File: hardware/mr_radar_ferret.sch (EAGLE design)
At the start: 66 parts, among them U1 GALI-55+, U10 MAX2750, U11 GALI-55+, U12 AD5621, U13 REF2930, U3 GALI-55+, U4 GALI-55+, U7 DC25-73, U8 HMC213

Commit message: mr_radar_ferret r0, sent for manufacturing
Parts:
- R22: value 110 -> JMP
- R23: value 110 -> DNP
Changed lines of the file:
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@@
 <part name="SUPPLY6" library="supply2" deviceset="+10V" device=""/>
 <part name="GND65" library="supply1" deviceset="GND" device=""/>
-<part name="R22" library="pel_dipol_comp" deviceset="RESISTOR" device="-0603" value="110"/>
+<part name="R22" library="pel_dipol_comp" deviceset="RESISTOR" device="-0603" value="JMP"/>
 <part name="P+18" library="supply1" deviceset="+5V" device=""/>
-<part name="R23" library="pel_dipol_comp" deviceset="RESISTOR" device="-0603" value="110"/>
+<part name="R23" library="pel_dipol_comp" deviceset="RESISTOR" device="-0603" value="DNP"/>
 <part name="GND70" library="supply1" deviceset="GND" device=""/>
 </parts>
@@
 <instance part="GND39" gate="1" x="-170.18" y="-71.12" rot="R90"/>
 <instance part="JP1" gate="G$1" x="-193.04" y="-73.66"/>
-<instance part="P+13" gate="1" x="81.28" y="109.22"/>
+<instance part="P+13" gate="1" x="78.74" y="101.6"/>
 <instance part="C30" gate="G$1" x="78.74" y="88.9"/>
 <instance part="GND47" gate="1" x="78.74" y="78.74"/>
@@
 <instance part="GND61" gate="1" x="53.34" y="78.74"/>
 <instance part="C20" gate="G$1" x="-20.32" y="-76.2"/>
-<instance part="P+14" gate="1" x="-20.32" y="-71.12"/>
-<instance part="GND62" gate="1" x="-20.32" y="-83.82"/>
+<instance part="P+14" gate="1" x="-20.32" y="-68.58"/>
+<instance part="GND62" gate="1" x="-20.32" y="-86.36"/>
 <instance part="J$5" gate="1" x="175.26" y="119.38" rot="MR0"/>
 <instance part="GND63" gate="1" x="180.34" y="99.06"/>
@@
 <pinref part="C20" gate="G$1" pin="2"/>
 <pinref part="GND62" gate="1" pin="GND"/>
+<wire x1="-20.32" y1="-83.82" x2="-20.32" y2="-81.28" width="0.1524" layer="91"/>
 </segment>
 <segment>
@@
 <segment>
 <pinref part="P+13" gate="1" pin="+5V"/>
-<wire x1="81.28" y1="106.68" x2="81.28" y2="99.06" width="0.1524" layer="91"/>
-<wire x1="81.28" y1="99.06" x2="78.74" y2="96.52" width="0.1524" layer="91"/>
 <pinref part="C30" gate="G$1" pin="+"/>
-<wire x1="78.74" y1="96.52" x2="78.74" y2="91.44" width="0.1524" layer="91"/>
+<wire x1="78.74" y1="99.06" x2="78.74" y2="91.44" width="0.1524" layer="91"/>
 </segment>
 <segment>
 <pinref part="C20" gate="G$1" pin="1"/>
 <pinref part="P+14" gate="1" pin="+5V"/>
-</segment>
-<segment>
+<wire x1="-20.32" y1="-71.12" x2="-20.32" y2="-73.66" width="0.1524" layer="91"/>
+</segment>
+<segment>

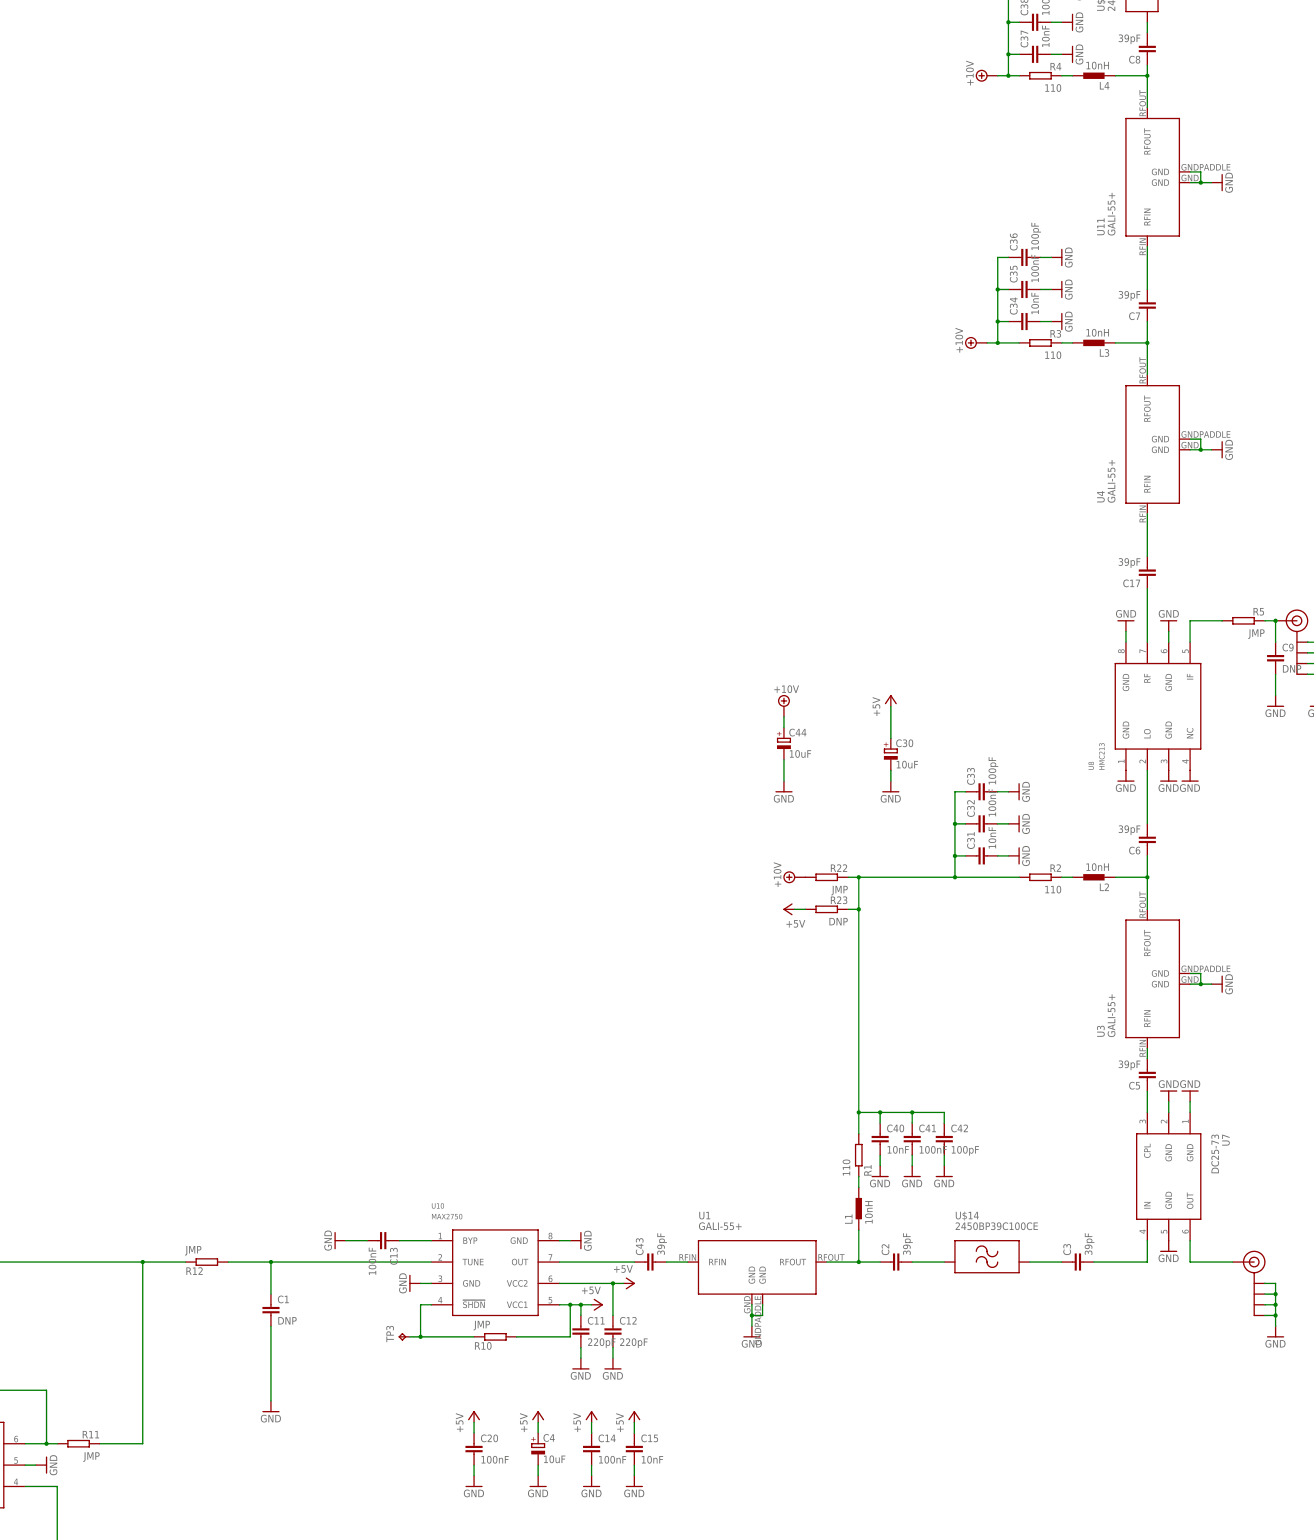
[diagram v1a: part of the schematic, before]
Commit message: currently tested ferret r0, fixing a few bugs for the next revision, board layout of ferret now incomplete. isolation is much better than in platypus, but it is still a problem
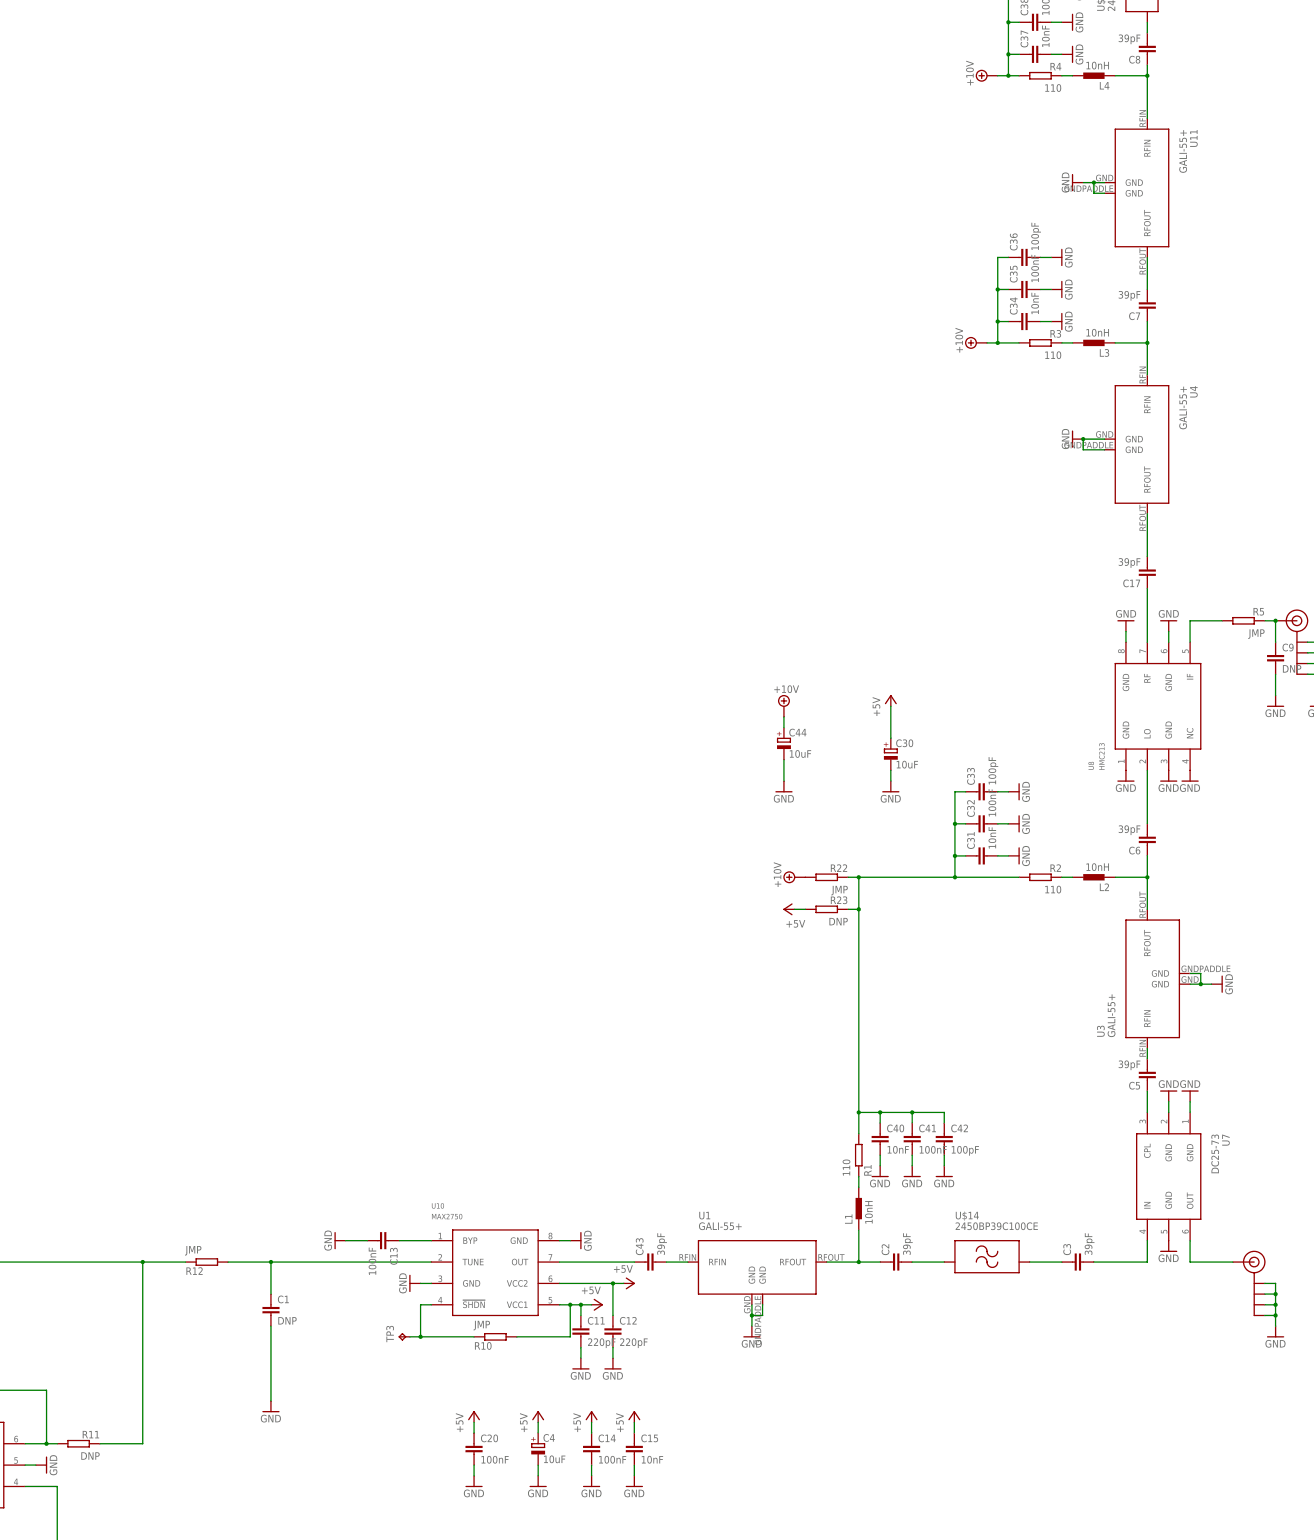
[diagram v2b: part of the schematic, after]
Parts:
- R11: value JMP -> DNP
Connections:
- removed net N$19: C7.2, U11.RFIN
- removed net N$29: C17.2, U4.RFIN
- new net N$23: C7.2, U11.RFOUT
- new net N$9: C17.2, U4.RFOUT
- net N$18: now also U4.RFIN; no longer U4.RFOUT
- net N$20: now also U11.RFIN; no longer U11.RFOUT
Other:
- moved on the sheet: U11, U4
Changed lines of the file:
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@@
 <part name="GND37" library="supply1" deviceset="GND" device=""/>
 <part name="GND38" library="supply1" deviceset="GND" device=""/>
-<part name="R11" library="pel_dipol_comp" deviceset="RESISTOR" device="-0603" value="JMP"/>
+<part name="R11" library="pel_dipol_comp" deviceset="RESISTOR" device="-0603" value="DNP"/>
 <part name="GND39" library="supply1" deviceset="GND" device=""/>
 <part name="JP1" library="SparkFun-Connectors" deviceset="M05" device="PTH"/>
@@
 <instance part="GND9" gate="1" x="134.62" y="119.38" rot="R180"/>
 <instance part="GND10" gate="1" x="144.78" y="119.38" rot="R180"/>
-<instance part="U4" gate="G$1" x="142.24" y="160.02" rot="R90"/>
+<instance part="U4" gate="G$1" x="137.16" y="162.56" rot="R270"/>
 <instance part="R3" gate="G$1" x="114.3" y="185.42" rot="R180"/>
 <instance part="L3" gate="G$1" x="127" y="185.42" rot="R90"/>
-<instance part="GND11" gate="1" x="157.48" y="160.02" rot="R90"/>
+<instance part="GND11" gate="1" x="121.92" y="162.56" rot="R270"/>
 <instance part="C7" gate="G$1" x="139.7" y="193.04" rot="R180"/>
 <instance part="SUPPLY3" gate="G$1" x="99.06" y="185.42" rot="R90"/>
-<instance part="U11" gate="G$1" x="142.24" y="223.52" rot="R90"/>
+<instance part="U11" gate="G$1" x="137.16" y="223.52" rot="R270"/>
 <instance part="R4" gate="G$1" x="114.3" y="248.92" rot="R180"/>
 <instance part="L4" gate="G$1" x="127" y="248.92" rot="R90"/>
-<instance part="GND12" gate="1" x="157.48" y="223.52" rot="R90"/>
+<instance part="GND12" gate="1" x="121.92" y="223.52" rot="R270"/>
 <instance part="C8" gate="G$1" x="139.7" y="254" rot="R180"/>
 <instance part="SUPPLY4" gate="G$1" x="101.6" y="248.92" rot="R90"/>
@@
 </segment>
 <segment>
-<pinref part="GND11" gate="1" pin="GND"/>
-<pinref part="U4" gate="G$1" pin="GND@0"/>
-<wire x1="154.94" y1="160.02" x2="152.4" y2="160.02" width="0.1524" layer="91"/>
-<pinref part="U4" gate="G$1" pin="GND@1"/>
-<wire x1="152.4" y1="160.02" x2="149.86" y2="160.02" width="0.1524" layer="91"/>
-<wire x1="149.86" y1="162.56" x2="152.4" y2="162.56" width="0.1524" layer="91"/>
-<wire x1="152.4" y1="162.56" x2="152.4" y2="160.02" width="0.1524" layer="91"/>
-<junction x="152.4" y="160.02"/>
-</segment>
-<segment>
 <pinref part="GND12" gate="1" pin="GND"/>
 <pinref part="U11" gate="G$1" pin="GND@0"/>
-<wire x1="154.94" y1="223.52" x2="152.4" y2="223.52" width="0.1524" layer="91"/>
+<wire x1="124.46" y1="223.52" x2="127" y2="223.52" width="0.1524" layer="91"/>
 <pinref part="U11" gate="G$1" pin="GND@1"/>
-<wire x1="152.4" y1="223.52" x2="149.86" y2="223.52" width="0.1524" layer="91"/>
-<wire x1="149.86" y1="226.06" x2="152.4" y2="226.06" width="0.1524" layer="91"/>
-<wire x1="152.4" y1="226.06" x2="152.4" y2="223.52" width="0.1524" layer="91"/>
-<junction x="152.4" y="223.52"/>
+<wire x1="127" y1="223.52" x2="129.54" y2="223.52" width="0.1524" layer="91"/>
+<wire x1="129.54" y1="220.98" x2="127" y2="220.98" width="0.1524" layer="91"/>
+<wire x1="127" y1="220.98" x2="127" y2="223.52" width="0.1524" layer="91"/>
+<junction x="127" y="223.52"/>
 </segment>
 <segment>
@@
 <pinref part="GND70" gate="1" pin="GND"/>
 </segment>
+<segment>
+<pinref part="GND11" gate="1" pin="GND"/>
+<pinref part="U4" gate="G$1" pin="GND@0"/>
+<wire x1="124.46" y1="162.56" x2="129.54" y2="162.56" width="0.1524" layer="91"/>
+<pinref part="U4" gate="G$1" pin="GND@1"/>
+<wire x1="129.54" y1="160.02" x2="124.46" y2="160.02" width="0.1524" layer="91"/>
+<wire x1="124.46" y1="160.02" x2="124.46" y2="162.56" width="0.1524" layer="91"/>
+<junction x="124.46" y="162.56"/>
+</segment>
 </net>
 <net name="N$2" class="0">
@@
 <net name="N$18" class="0">
 <segment>
-<pinref part="U4" gate="G$1" pin="RFOUT"/>
 <pinref part="C7" gate="G$1" pin="1"/>
-<wire x1="139.7" y1="177.8" x2="139.7" y2="185.42" width="0.1524" layer="91"/>
 <pinref part="L3" gate="G$1" pin="2"/>
 <wire x1="139.7" y1="185.42" x2="139.7" y2="190.5" width="0.1524" layer="91"/>
 <wire x1="132.08" y1="185.42" x2="139.7" y2="185.42" width="0.1524" layer="91"/>
+<pinref part="U4" gate="G$1" pin="RFIN"/>
+<wire x1="139.7" y1="177.8" x2="139.7" y2="185.42" width="0.1524" layer="91"/>
 <junction x="139.7" y="185.42"/>
 </segment>
@@
 <net name="N$20" class="0">
 <segment>
-<pinref part="U11" gate="G$1" pin="RFOUT"/>
 <pinref part="C8" gate="G$1" pin="1"/>
-<wire x1="139.7" y1="241.3" x2="139.7" y2="248.92" width="0.1524" layer="91"/>
 <pinref part="L4" gate="G$1" pin="2"/>
 <wire x1="139.7" y1="248.92" x2="139.7" y2="251.46" width="0.1524" layer="91"/>
 <wire x1="132.08" y1="248.92" x2="139.7" y2="248.92" width="0.1524" layer="91"/>
+<wire x1="139.7" y1="238.76" x2="139.7" y2="248.92" width="0.1524" layer="91"/>
 <junction x="139.7" y="248.92"/>
-</segment>
-</net>
-<net name="N$19" class="0">
-<segment>
 <pinref part="U11" gate="G$1" pin="RFIN"/>
-<wire x1="139.7" y1="208.28" x2="139.7" y2="198.12" width="0.1524" layer="91"/>
-<pinref part="C7" gate="G$1" pin="2"/>
 </segment>
 </net>
@@
 <pinref part="U8" gate="G$1" pin="RF@7"/>
 <wire x1="139.7" y1="127" x2="139.7" y2="114.3" width="0.1524" layer="91"/>
-</segment>
-</net>
-<net name="N$29" class="0">
-<segment>
-<pinref part="C17" gate="G$1" pin="2"/>
-<pinref part="U4" gate="G$1" pin="RFIN"/>
-<wire x1="139.7" y1="134.62" x2="139.7" y2="144.78" width="0.1524" layer="91"/>
 </segment>
 </net>
@@
 </segment>
 </net>
+<net name="N$9" class="0">
+<segment>
+<pinref part="U4" gate="G$1" pin="RFOUT"/>
+<wire x1="139.7" y1="144.78" x2="139.7" y2="134.62" width="0.1524" layer="91"/>
+<pinref part="C17" gate="G$1" pin="2"/>
+</segment>
+</net>
+<net name="N$23" class="0">
+<segment>
+<pinref part="C7" gate="G$1" pin="2"/>
+<pinref part="U11" gate="G$1" pin="RFOUT"/>
+<wire x1="139.7" y1="198.12" x2="139.7" y2="205.74" width="0.1524" layer="91"/>
+</segment>
+</net>
